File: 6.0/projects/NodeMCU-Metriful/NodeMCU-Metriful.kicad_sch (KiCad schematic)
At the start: 5 parts, among them J3 DS18b20 connector, J4 Conn_01x03_Female, U1 NodeMCU_1.0_(ESP-12E), U2 Metriful-1

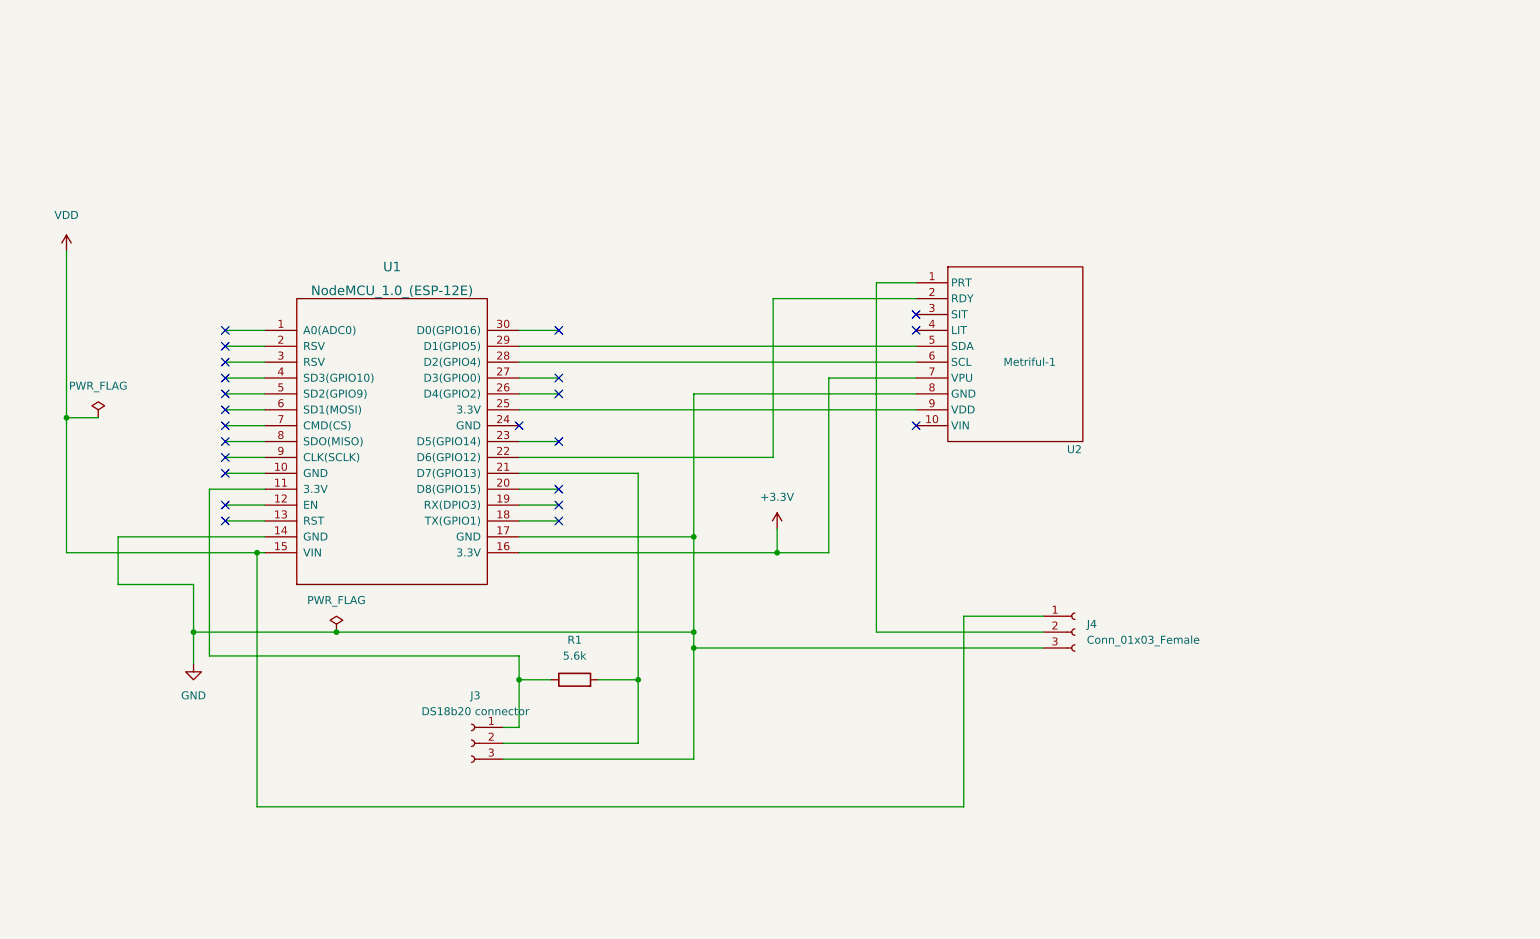
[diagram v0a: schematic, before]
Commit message: Add NodeMCU-Metriful project
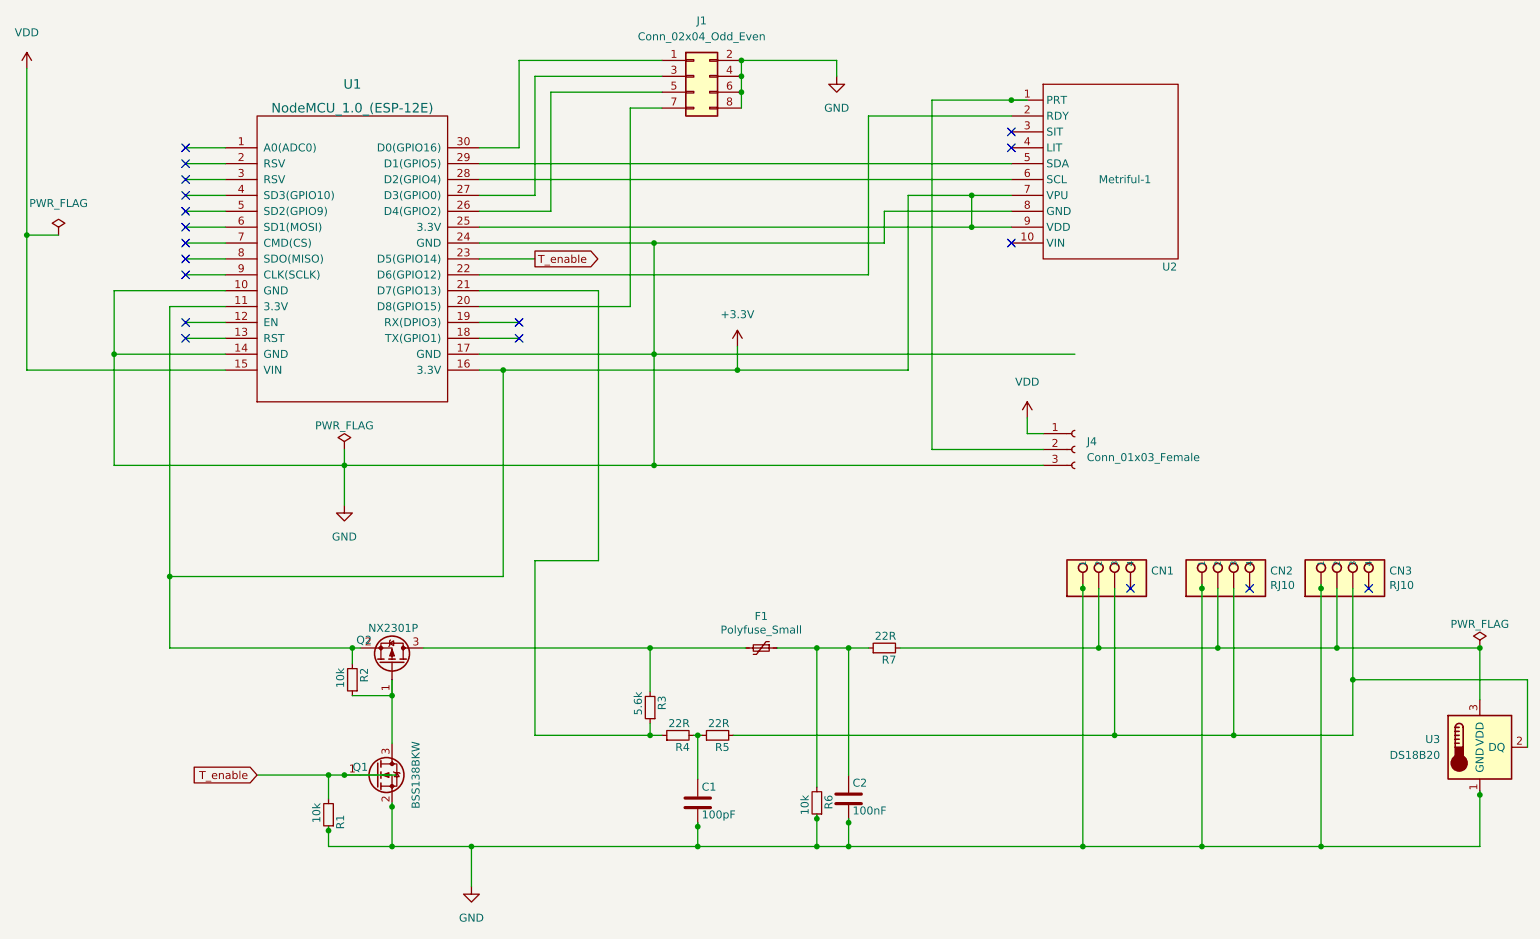
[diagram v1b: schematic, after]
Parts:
- removed J3: DS18b20 connector, Connector_JST:JST_PH_B3B-PH-K_1x03_P2.00mm_Vertical, symbol Connector:Conn_01x03_Female
- removed R1: 5.6k, Resistor_SMD:R_1210_3225Metric_Pad1.30x2.65mm_HandSolder, symbol Device:R
- added C1: 100pF, Capacitor_SMD:C_0805_2012Metric_Pad1.18x1.45mm_HandSolder, symbol 1wire-v0.4:Device_C
- added C2: 100nF, Capacitor_SMD:C_0805_2012Metric, symbol 1wire-v0.4:Device_C
- added CN1: (no value), symbol 1wire-v0.4:RJ10
- added CN2, CN3: RJ10, symbol 1wire-v0.4:RJ10
- added F1: Polyfuse_Small, Fuse:Fuse_1210_3225Metric_Pad1.42x2.65mm_HandSolder, symbol 1wire-v0.4:Polyfuse_Small
- added J1: Conn_02x04_Odd_Even, Connector_PinHeader_2.54mm:PinHeader_2x04_P2.54mm_Vertical, symbol Connector_Generic:Conn_02x04_Odd_Even
- added Q1: BSS138BKW, Package_TO_SOT_SMD:SOT-323_SC-70_Handsoldering, symbol 1wire-v0.4:Device_Q_NMOS_GSD
- added Q2: NX2301P, 1wire-v0.4:SOT-23-3, symbol 1wire-v0.4:Device_Q_PMOS_GSD
- added R1, R2, R6: 10k, Resistor_SMD:R_0805_2012Metric_Pad1.20x1.40mm_HandSolder, symbol 1wire-v0.4:Device_R_Small
- added R3: 5.6k, Resistor_SMD:R_0805_2012Metric_Pad1.20x1.40mm_HandSolder, symbol 1wire-v0.4:Device_R_Small
- added R4, R5, R7: 22R, Resistor_SMD:R_0805_2012Metric_Pad1.20x1.40mm_HandSolder, symbol 1wire-v0.4:Device_R_Small
- added U3: DS18B20, Package_TO_SOT_THT:TO-92_Inline, symbol Sensor_Temperature:DS18B20
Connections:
- net +3V3: now also U1.11 (3.3V), U1.25 (3.3V), U2.9 (VDD), Q2.2 (S), R2.2
- net GND: now also U1.10 (GND), U1.24 (GND), C1.2, C2.2, CN1.1, CN2.1, CN3.1, J1.2 (Pin_2), J1.4 (Pin_4), J1.6 (Pin_6), J1.8 (Pin_8), Q1.2 (S), R1.1, R6.1, U3.1 (GND)
- net at U1.21 (D7(GPIO13)): now also R3.1, R4.1
- net at U1.20 (D8(GPIO15)): now also J1.7 (Pin_7)
- net T_enable: now reaches U1.23 (D5(GPIO14))
- net T_enable: now also Q1.1 (G), R1.2
- net at U1.26 (D4(GPIO2)): now also J1.5 (Pin_5)
- net at U1.27 (D3(GPIO0)): now also J1.3 (Pin_3)
- net at U1.30 (D0(GPIO16)): now also J1.1 (Pin_1)
- new net: Q1.3 (D), Q2.1 (G), R2.1
- new net: F1.2, Q2.3 (D), R3.2
- new net: C2.1, F1.1, R6.2, R7.1
- new net: CN1.2, CN2.2, CN3.2, R7.2, U3.3 (VDD)
- new net: CN1.3, CN2.3, CN3.3, R5.2, U3.2 (DQ)
- new net: C1.1, R4.2, R5.1
- no-connect marks 23 -> 19
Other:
- company: (none) -> Phluxus
- title: (none) -> NodeMCU-Metriful
- moved on the sheet: J4, U1, U2
